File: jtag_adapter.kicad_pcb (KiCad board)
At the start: 2 copper layers, 50 x 50 mm, 18 parts, among them J1 Conn_ARM_JTAG_SWD_10, J2 Conn_ARM_JTAG_SWD_20, J3 Conn_ARM_JTAG_SWD_10, J4 Conn_ARM_JTAG_SWD_20, J5 Conn_ARM_JTAG_SWD_20, J6 AVR-JTAG-10, J7 AVR-ISP-6, J8 AVR-ISP-10, J9 AVR-ISP-10, Q1 BSS138, Q2 BSS138

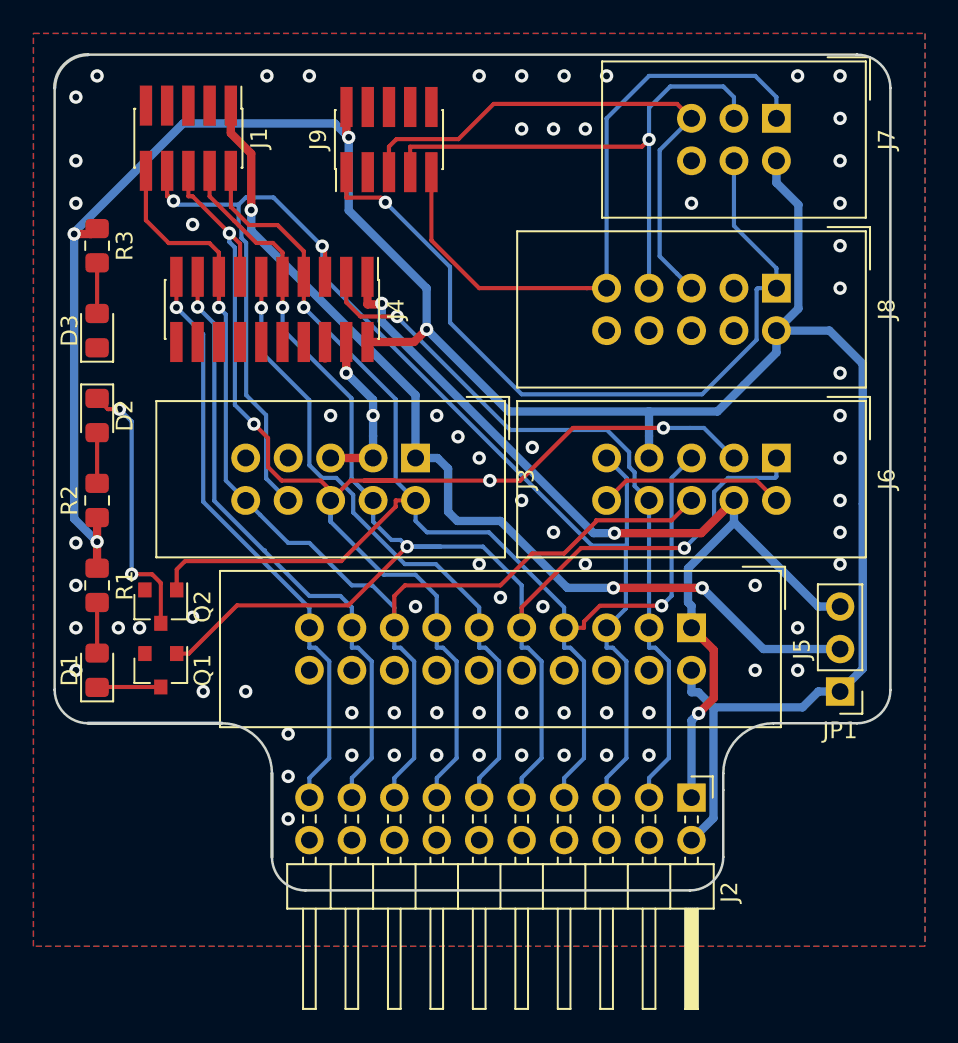
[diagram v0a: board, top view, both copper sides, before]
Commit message: small schematic fix and created silkscreen printings
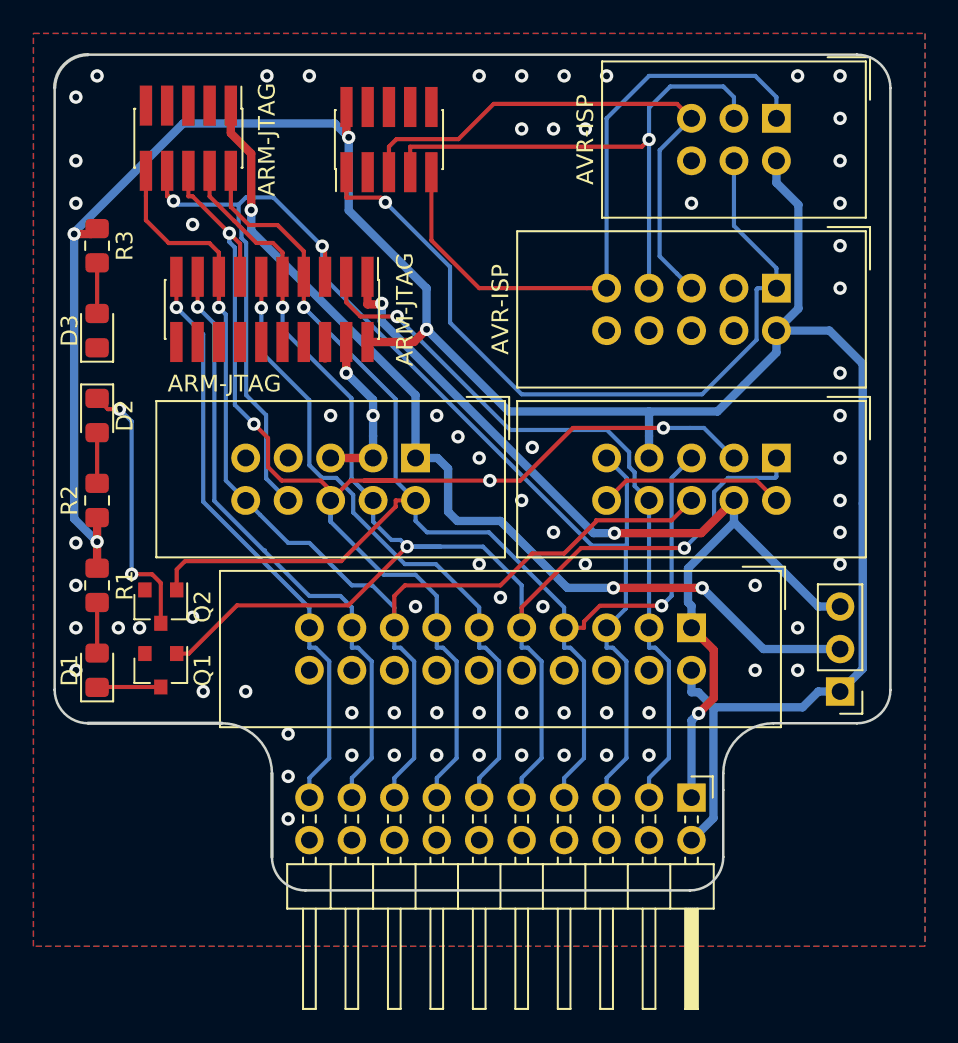
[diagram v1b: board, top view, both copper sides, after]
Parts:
- added REF**: KiCad-Logo2_6mm_SilkScreen, Symbol:KiCad-Logo2_6mm_SilkScreen, B.Cu at (130.2, 78.1)
- added REF**: OSHW-Logo2_9.8x8mm_SilkScreen, Symbol:OSHW-Logo2_9.8x8mm_SilkScreen, B.Cu at (123.2, 69.8)
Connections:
- J6 pad 10: Net-(J6-Pad10) -> GND
- J6 pad 2: Net-(J6-Pad10) -> GND
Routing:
- net GND: track 15.8 -> 26.9 mm
- net Net-(J6-Pad10): track 11.1 -> 0.00 mm
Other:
- board text added: "ACK"
- board text added: "ARM-JTAG"
- board text added: "ATMEL JTAG"
- board text added: "AVR-ISP"
- board text added: "DBxxx"
- board text added: "GND"
- board text added: "JTAG"
- board text added: "MISO"
- board text added: "MOSI"
- board text added: "RQ"
- board text added: "RST"
- board text added: "RTCK"
- board text added: "SCK"
- board text added: "SRST"
- board text added: "SWD"
- board text added: "SWIO SWO SWCLK"
- board text added: "TCK"
- board text added: "TDI"
- board text added: "TDO"
- board text added: "TMS"
- board text added: "TMS TDO TCK"
- board text added: "TRST"
- board text added: "VCC"
- board text added: "VTREF"
